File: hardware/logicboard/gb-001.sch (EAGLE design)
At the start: 6 parts

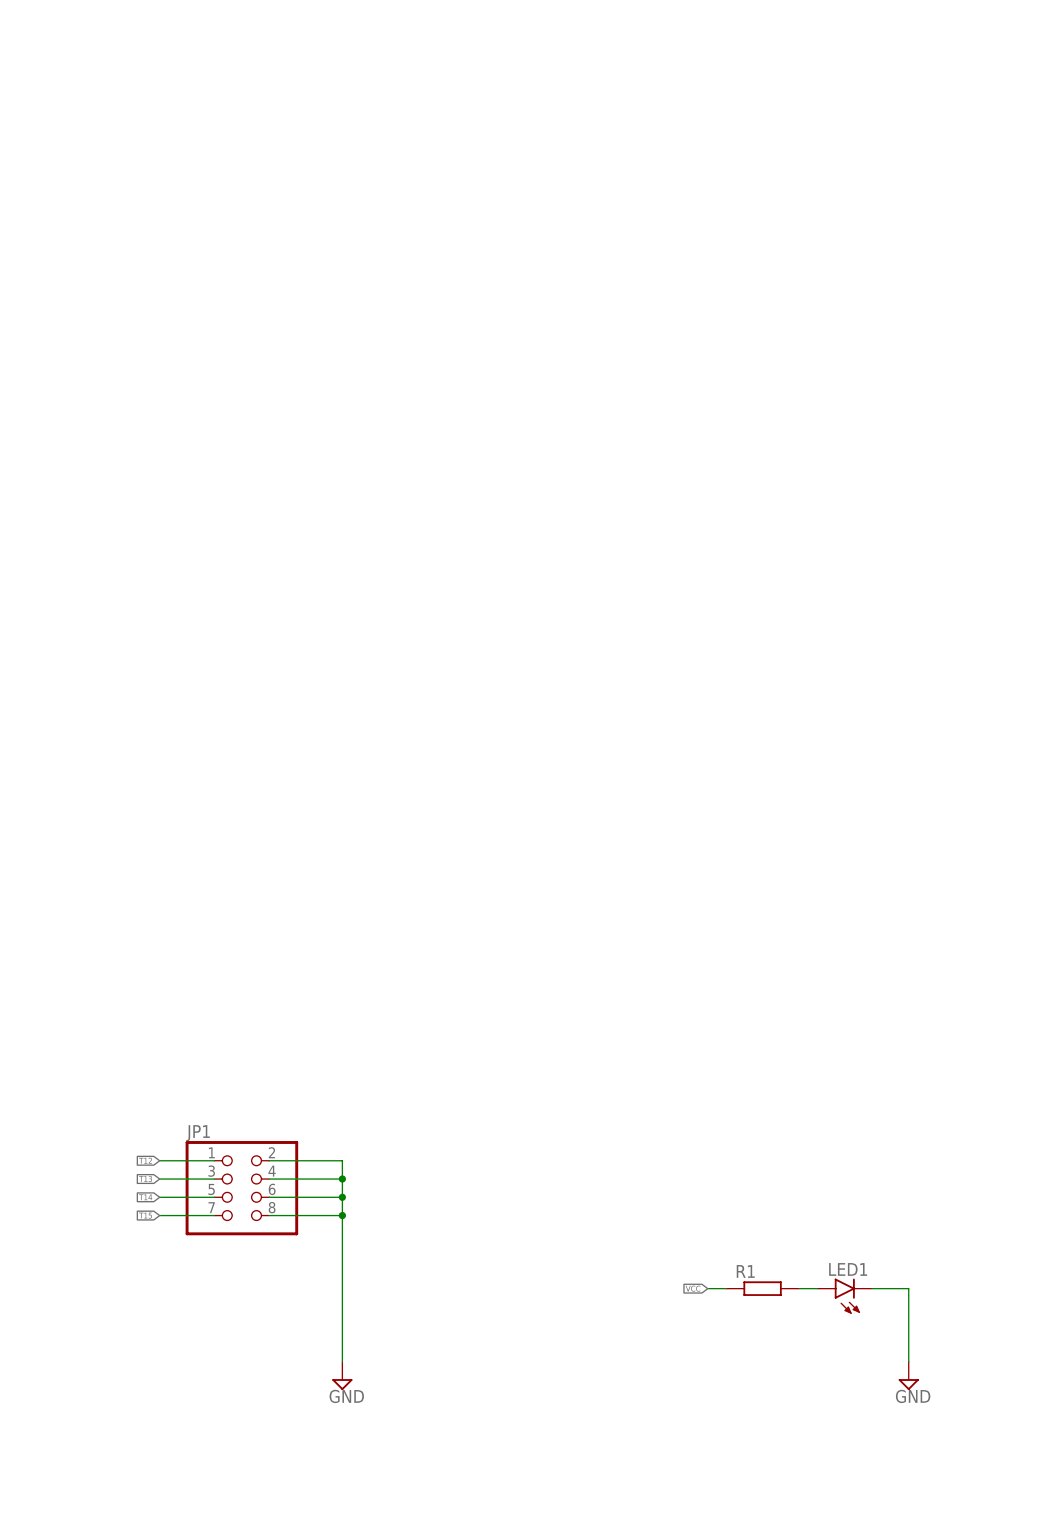
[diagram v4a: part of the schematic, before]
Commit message: Added GeekPort.
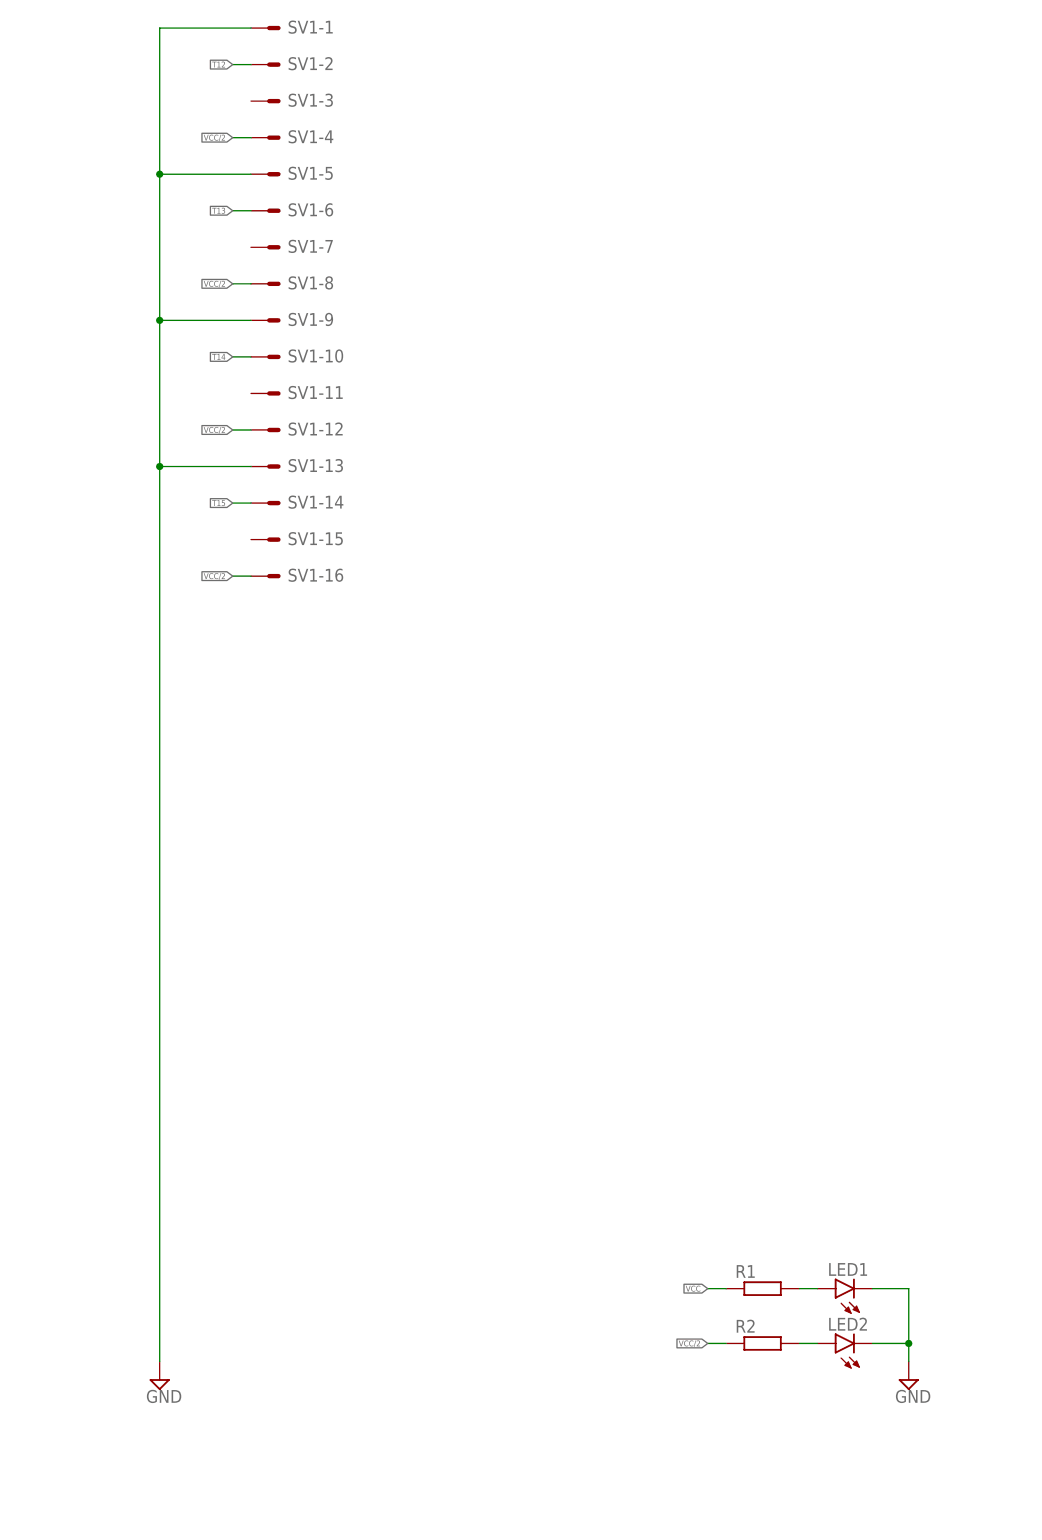
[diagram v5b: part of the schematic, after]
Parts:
- removed JP1: (no value), pinhead:PINHD-2X4
- added LED2: (no value), led:LED3MM
- added R2: (no value), rcl:R-EU_0204/5
- added SV1: (no value), con-ml:ML16LE
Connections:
- new net N$1: LED2.A, R2.2
- new net VCC/2: R2.1, SV1-12.S, SV1-16.S, SV1-4.S, SV1-8.S
- net GND: now also LED2.C, SV1-1.S, SV1-13.S, SV1-5.S, SV1-9.S; no longer JP1.2, JP1.4, JP1.6, JP1.8
- net T12: now also SV1-2.S; no longer JP1.1
- net T13: now also SV1-6.S; no longer JP1.3
- net T14: now also SV1-10.S; no longer JP1.5
- net T15: now also SV1-14.S; no longer JP1.7

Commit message: Added signal names and silk patterns.
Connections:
- net N$1 renamed VCC2LED
- net N$2 renamed VCCLED
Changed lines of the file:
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@@
 </segment>
 </net>
-<net name="N$2" class="0">
+<net name="VCCLED" class="0">
 <segment>
 <pinref part="R1" gate="G$1" pin="2"/>
@@
 </segment>
 </net>
-<net name="N$1" class="0">
+<net name="VCC2LED" class="0">
 <segment>
 <pinref part="LED2" gate="G$1" pin="A"/>

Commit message: Renamed signals.
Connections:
- net T00 renamed GB00
- net T01 renamed GB01
- net T02 renamed GB02
- net T03 renamed GB03
- net T04 renamed GB04
- net T05 renamed GB05
- net T06 renamed GB06
- net T07 renamed GB07
- net T08 renamed GB08
- net T09 renamed GB09
- net T10 renamed GB10
- net T11 renamed GB11
- net T12 renamed GB12
- net T13 renamed GB13
- net T14 renamed GB14
- net T15 renamed GB15
- removed net NC: SV0-17.S
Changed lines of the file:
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@@
 </segment>
 </net>
-<net name="T00" class="0">
+<net name="GB00" class="0">
 <segment>
 <pinref part="SV0" gate="-1" pin="S"/>
@@
 </segment>
 </net>
-<net name="T01" class="0">
+<net name="GB01" class="0">
 <segment>
 <pinref part="SV0" gate="-3" pin="S"/>
@@
 </segment>
 </net>
-<net name="T02" class="0">
+<net name="GB02" class="0">
 <segment>
 <pinref part="SV0" gate="-5" pin="S"/>
@@
 </segment>
 </net>
-<net name="T03" class="0">
+<net name="GB03" class="0">
 <segment>
 <pinref part="SV0" gate="-7" pin="S"/>
@@
 </segment>
 </net>
-<net name="T04" class="0">
+<net name="GB04" class="0">
 <segment>
 <pinref part="SV0" gate="-9" pin="S"/>
@@
 </segment>
 </net>
-<net name="T05" class="0">
+<net name="GB05" class="0">
 <segment>
 <pinref part="SV0" gate="-11" pin="S"/>
@@
 </segment>
 </net>
-<net name="T06" class="0">
+<net name="GB06" class="0">
 <segment>
 <pinref part="SV0" gate="-13" pin="S"/>
@@
 </segment>
 </net>
-<net name="T07" class="0">
+<net name="GB07" class="0">
 <segment>
 <pinref part="SV0" gate="-15" pin="S"/>
@@
 </segment>
 </net>
-<net name="NC" class="0">
-<segment>
-<pinref part="SV0" gate="-17" pin="S"/>
-<wire x1="35.56" y1="162.56" x2="33.02" y2="162.56" width="0.1524" layer="91"/>
-<label x="33.02" y="162.56" size="0.8128" layer="95" rot="R180" xref="yes"/>
-</segment>
-</net>
-<net name="T08" class="0">
+<net name="GB08" class="0">
 <segment>
 <pinref part="SV0" gate="-19" pin="S"/>
@@
 </segment>
 </net>
-<net name="T09" class="0">
+<net name="GB09" class="0">
 <segment>
 <pinref part="SV0" gate="-21" pin="S"/>
@@
 </segment>
 </net>
-<net name="T10" class="0">
+<net name="GB10" class="0">
 <segment>
 <pinref part="SV0" gate="-23" pin="S"/>
@@
 </segment>
 </net>
-<net name="T11" class="0">
+<net name="GB11" class="0">
 <segment>
 <pinref part="SV0" gate="-25" pin="S"/>
@@
 </segment>
 </net>
-<net name="T12" class="0">
+<net name="GB12" class="0">
 <segment>
 <pinref part="SV0" gate="-27" pin="S"/>
@@
 </segment>
 </net>
-<net name="T13" class="0">
+<net name="GB13" class="0">
 <segment>
 <pinref part="SV0" gate="-29" pin="S"/>
@@
 </segment>
 </net>
-<net name="T14" class="0">
+<net name="GB14" class="0">
 <segment>
 <pinref part="SV0" gate="-31" pin="S"/>
@@
 </segment>
 </net>
-<net name="T15" class="0">
+<net name="GB15" class="0">
 <segment>
 <pinref part="SV0" gate="-33" pin="S"/>

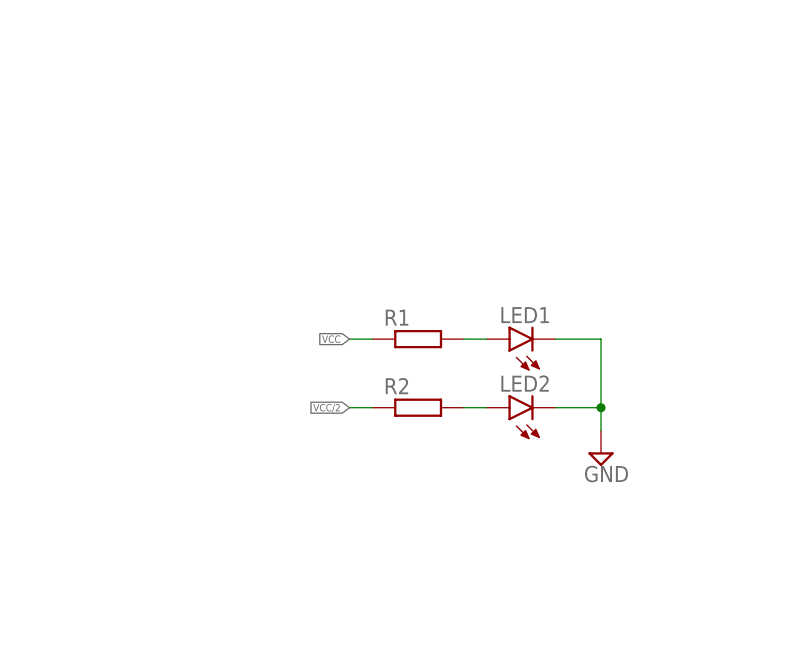
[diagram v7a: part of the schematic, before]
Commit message: Added capacitors.
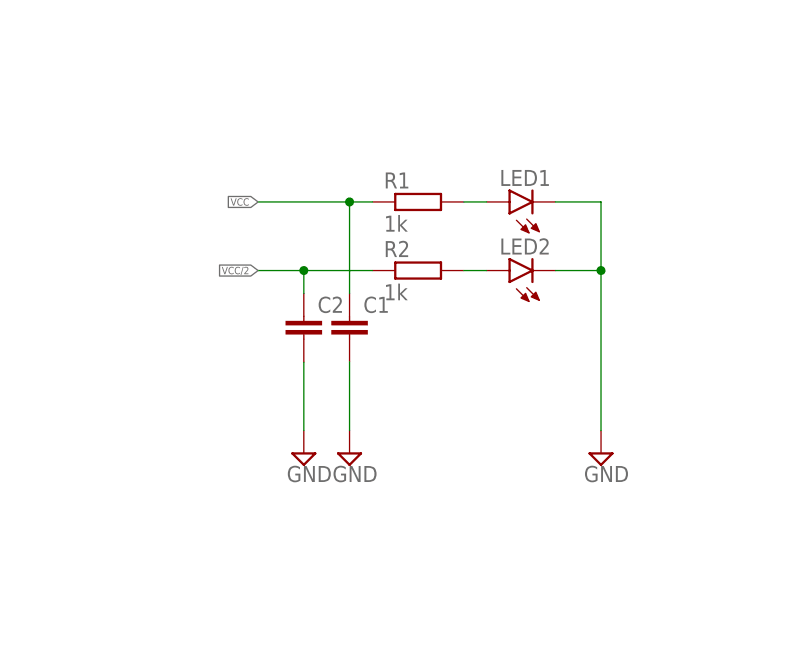
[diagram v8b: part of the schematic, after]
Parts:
- added C1, C2: (no value), rcl:C-EU025-025X050
- R1, R2: value (none) -> 1k
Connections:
- net GND: now also C1.2, C2.2
- net VCC: now also C1.1
- net VCC/2: now also C2.1
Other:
- moved on the sheet: LED1, LED2, R1, R2
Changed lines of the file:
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@@
 <part name="SUPPLY3" library="supply2" library_urn="urn:adsk.eagle:library:372" deviceset="GND" device=""/>
 <part name="SUPPLY2" library="supply2" library_urn="urn:adsk.eagle:library:372" deviceset="GND" device=""/>
-<part name="R1" library="rcl" library_urn="urn:adsk.eagle:library:334" deviceset="R-EU_" device="0204/5" package3d_urn="urn:adsk.eagle:package:23488/1"/>
+<part name="R1" library="rcl" library_urn="urn:adsk.eagle:library:334" deviceset="R-EU_" device="0204/5" package3d_urn="urn:adsk.eagle:package:23488/1" value="1k"/>
 <part name="LED1" library="led" library_urn="urn:adsk.eagle:library:259" deviceset="LED" device="3MM" package3d_urn="urn:adsk.eagle:package:15797/1"/>
 <part name="SUPPLY4" library="supply2" library_urn="urn:adsk.eagle:library:372" deviceset="GND" device=""/>
 <part name="SV1" library="con-ml" library_urn="urn:adsk.eagle:library:164" deviceset="ML16LE" device="" package3d_urn="urn:adsk.eagle:package:8682/1"/>
-<part name="R2" library="rcl" library_urn="urn:adsk.eagle:library:334" deviceset="R-EU_" device="0204/5" package3d_urn="urn:adsk.eagle:package:23488/1"/>
+<part name="R2" library="rcl" library_urn="urn:adsk.eagle:library:334" deviceset="R-EU_" device="0204/5" package3d_urn="urn:adsk.eagle:package:23488/1" value="1k"/>
 <part name="LED2" library="led" library_urn="urn:adsk.eagle:library:259" deviceset="LED" device="3MM" package3d_urn="urn:adsk.eagle:package:15797/1"/>
+<part name="C1" library="rcl" library_urn="urn:adsk.eagle:library:334" deviceset="C-EU" device="025-025X050" package3d_urn="urn:adsk.eagle:package:23629/2"/>
+<part name="C2" library="rcl" library_urn="urn:adsk.eagle:library:334" deviceset="C-EU" device="025-025X050" package3d_urn="urn:adsk.eagle:package:23629/2"/>
+<part name="SUPPLY5" library="supply2" library_urn="urn:adsk.eagle:library:372" deviceset="GND" device=""/>
+<part name="SUPPLY6" library="supply2" library_urn="urn:adsk.eagle:library:372" deviceset="GND" device=""/>
 </parts>
 <sheets>
@@
 <attribute name="VALUE" x="150.495" y="52.705" size="1.778" layer="96"/>
 </instance>
-<instance part="R1" gate="G$1" x="236.22" y="68.58" smashed="yes">
-<attribute name="NAME" x="232.41" y="70.0786" size="1.778" layer="95"/>
-<attribute name="VALUE" x="232.41" y="65.278" size="1.778" layer="96"/>
-</instance>
-<instance part="LED1" gate="G$1" x="246.38" y="68.58" smashed="yes" rot="R90">
-<attribute name="NAME" x="250.952" y="72.136" size="1.778" layer="95" rot="R180"/>
-<attribute name="VALUE" x="250.952" y="74.295" size="1.778" layer="96" rot="R180"/>
+<instance part="R1" gate="G$1" x="236.22" y="83.82" smashed="yes">
+<attribute name="NAME" x="232.41" y="85.3186" size="1.778" layer="95"/>
+<attribute name="VALUE" x="232.41" y="80.518" size="1.778" layer="96"/>
+</instance>
+<instance part="LED1" gate="G$1" x="246.38" y="83.82" smashed="yes" rot="R90">
+<attribute name="NAME" x="250.952" y="87.376" size="1.778" layer="95" rot="R180"/>
+<attribute name="VALUE" x="250.952" y="89.535" size="1.778" layer="96" rot="R180"/>
 </instance>
 <instance part="SUPPLY4" gate="GND" x="256.54" y="55.88" smashed="yes">
@@
 <attribute name="VALUE" x="167.386" y="164.719" size="1.778" layer="96"/>
 </instance>
-<instance part="R2" gate="G$1" x="236.22" y="60.96" smashed="yes">
-<attribute name="NAME" x="232.41" y="62.4586" size="1.778" layer="95"/>
-<attribute name="VALUE" x="232.41" y="57.658" size="1.778" layer="96"/>
-</instance>
-<instance part="LED2" gate="G$1" x="246.38" y="60.96" smashed="yes" rot="R90">
-<attribute name="NAME" x="250.952" y="64.516" size="1.778" layer="95" rot="R180"/>
-<attribute name="VALUE" x="250.952" y="66.675" size="1.778" layer="96" rot="R180"/>
+<instance part="R2" gate="G$1" x="236.22" y="76.2" smashed="yes">
+<attribute name="NAME" x="232.41" y="77.6986" size="1.778" layer="95"/>
+<attribute name="VALUE" x="232.41" y="72.898" size="1.778" layer="96"/>
+</instance>
+<instance part="LED2" gate="G$1" x="246.38" y="76.2" smashed="yes" rot="R90">
+<attribute name="NAME" x="250.952" y="79.756" size="1.778" layer="95" rot="R180"/>
+<attribute name="VALUE" x="250.952" y="81.915" size="1.778" layer="96" rot="R180"/>
+</instance>
+<instance part="C1" gate="G$1" x="228.6" y="71.12" smashed="yes">
+<attribute name="NAME" x="230.124" y="71.501" size="1.778" layer="95"/>
+<attribute name="VALUE" x="230.124" y="66.421" size="1.778" layer="96"/>
+</instance>
+<instance part="C2" gate="G$1" x="223.52" y="71.12" smashed="yes">
+<attribute name="NAME" x="225.044" y="71.501" size="1.778" layer="95"/>
+<attribute name="VALUE" x="225.044" y="66.421" size="1.778" layer="96"/>
+</instance>
+<instance part="SUPPLY5" gate="GND" x="228.6" y="55.88" smashed="yes">
+<attribute name="VALUE" x="226.695" y="52.705" size="1.778" layer="96"/>
+</instance>
+<instance part="SUPPLY6" gate="GND" x="223.52" y="55.88" smashed="yes">
+<attribute name="VALUE" x="221.615" y="52.705" size="1.778" layer="96"/>
 </instance>
 </instances>
@@
 <segment>
 <pinref part="LED1" gate="G$1" pin="C"/>
-<wire x1="251.46" y1="68.58" x2="256.54" y2="68.58" width="0.1524" layer="91"/>
+<wire x1="251.46" y1="83.82" x2="256.54" y2="83.82" width="0.1524" layer="91"/>
 <pinref part="SUPPLY4" gate="GND" pin="GND"/>
-<wire x1="256.54" y1="68.58" x2="256.54" y2="60.96" width="0.1524" layer="91"/>
+<wire x1="256.54" y1="83.82" x2="256.54" y2="76.2" width="0.1524" layer="91"/>
 <pinref part="LED2" gate="G$1" pin="C"/>
-<wire x1="256.54" y1="60.96" x2="256.54" y2="58.42" width="0.1524" layer="91"/>
-<wire x1="251.46" y1="60.96" x2="256.54" y2="60.96" width="0.1524" layer="91"/>
-<junction x="256.54" y="60.96"/>
+<wire x1="256.54" y1="76.2" x2="256.54" y2="58.42" width="0.1524" layer="91"/>
+<wire x1="251.46" y1="76.2" x2="256.54" y2="76.2" width="0.1524" layer="91"/>
+<junction x="256.54" y="76.2"/>
 </segment>
 <segment>
@@
 <pinref part="SUPPLY2" gate="GND" pin="GND"/>
 </segment>
+<segment>
+<pinref part="C2" gate="G$1" pin="2"/>
+<pinref part="SUPPLY6" gate="GND" pin="GND"/>
+<wire x1="223.52" y1="66.04" x2="223.52" y2="58.42" width="0.1524" layer="91"/>
+</segment>
+<segment>
+<pinref part="C1" gate="G$1" pin="2"/>
+<pinref part="SUPPLY5" gate="GND" pin="GND"/>
+<wire x1="228.6" y1="66.04" x2="228.6" y2="58.42" width="0.1524" layer="91"/>
+</segment>
 </net>
 <net name="GB00" class="0">
@@
 <segment>
 <pinref part="R1" gate="G$1" pin="1"/>
-<wire x1="228.6" y1="68.58" x2="231.14" y2="68.58" width="0.1524" layer="91"/>
-<label x="228.6" y="68.58" size="0.8128" layer="95" rot="R180" xref="yes"/>
+<wire x1="218.44" y1="83.82" x2="228.6" y2="83.82" width="0.1524" layer="91"/>
+<label x="218.44" y="83.82" size="0.8128" layer="95" rot="R180" xref="yes"/>
+<pinref part="C1" gate="G$1" pin="1"/>
+<wire x1="228.6" y1="83.82" x2="231.14" y2="83.82" width="0.1524" layer="91"/>
+<wire x1="228.6" y1="73.66" x2="228.6" y2="83.82" width="0.1524" layer="91"/>
+<junction x="228.6" y="83.82"/>
 </segment>
 </net>
@@
 <pinref part="R1" gate="G$1" pin="2"/>
 <pinref part="LED1" gate="G$1" pin="A"/>
-<wire x1="241.3" y1="68.58" x2="243.84" y2="68.58" width="0.1524" layer="91"/>
+<wire x1="241.3" y1="83.82" x2="243.84" y2="83.82" width="0.1524" layer="91"/>
 </segment>
 </net>
@@
 <pinref part="LED2" gate="G$1" pin="A"/>
 <pinref part="R2" gate="G$1" pin="2"/>
-<wire x1="243.84" y1="60.96" x2="241.3" y2="60.96" width="0.1524" layer="91"/>
+<wire x1="243.84" y1="76.2" x2="241.3" y2="76.2" width="0.1524" layer="91"/>
 </segment>
 </net>
@@
 <segment>
 <pinref part="R2" gate="G$1" pin="1"/>
-<wire x1="231.14" y1="60.96" x2="228.6" y2="60.96" width="0.1524" layer="91"/>
-<label x="228.6" y="60.96" size="0.8128" layer="95" rot="R180" xref="yes"/>
-</segment>
-<segment>
+<wire x1="231.14" y1="76.2" x2="223.52" y2="76.2" width="0.1524" layer="91"/>
+<label x="218.44" y="76.2" size="0.8128" layer="95" rot="R180" xref="yes"/>
+<pinref part="C2" gate="G$1" pin="1"/>
+<wire x1="223.52" y1="76.2" x2="218.44" y2="76.2" width="0.1524" layer="91"/>
+<wire x1="223.52" y1="73.66" x2="223.52" y2="76.2" width="0.1524" layer="91"/>
+<junction x="223.52" y="76.2"/>
+</segment>
+<segment>
